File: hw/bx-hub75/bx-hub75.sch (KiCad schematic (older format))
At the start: 11 parts, among them J1 DB9_Male, U1 74HCT541, U2 74HCT541, U3 LD1117S33TR_SOT223, U4 25LCxxx, U5 SN65HVD77D

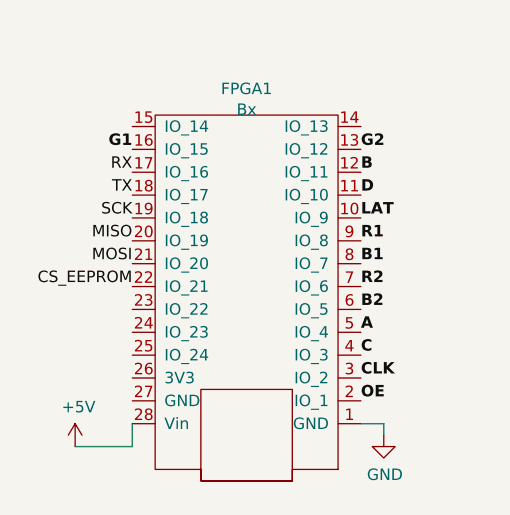
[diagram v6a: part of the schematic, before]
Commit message: hw/bx-hub75: finish basic routing.
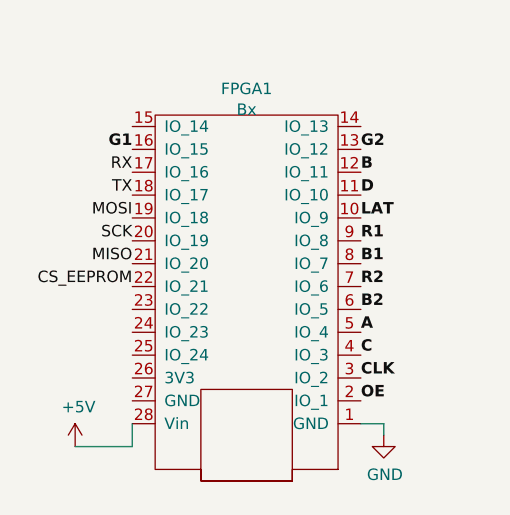
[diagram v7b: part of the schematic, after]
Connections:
- net MISO: now also FPGA1.21 (IO_20); no longer FPGA1.20 (IO_19)
- net MOSI: now also FPGA1.19 (IO_18); no longer FPGA1.21 (IO_20)
- net SCK: now also FPGA1.20 (IO_19); no longer FPGA1.19 (IO_18)
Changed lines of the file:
@@
 Connection ~ 4700 5000
 Text Label 2350 2550 2    50   ~ 0
+MOSI
+Text Label 2350 2650 2    50   ~ 0
 SCK
-Text Label 2350 2650 2    50   ~ 0
+Text Label 2350 2750 2    50   ~ 0
 MISO
-Text Label 2350 2750 2    50   ~ 0
-MOSI
 Text Label 2350 2850 2    50   ~ 0
 CS_EEPROM

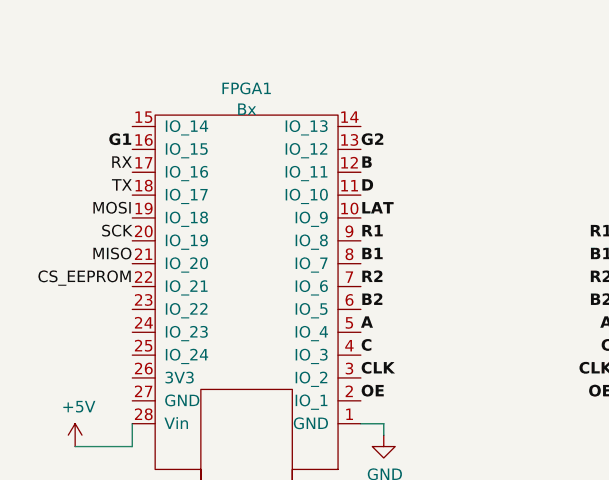
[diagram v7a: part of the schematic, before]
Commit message: hw/{library,bx-hub75}: TinyFPGA has 28 pins, not 26...
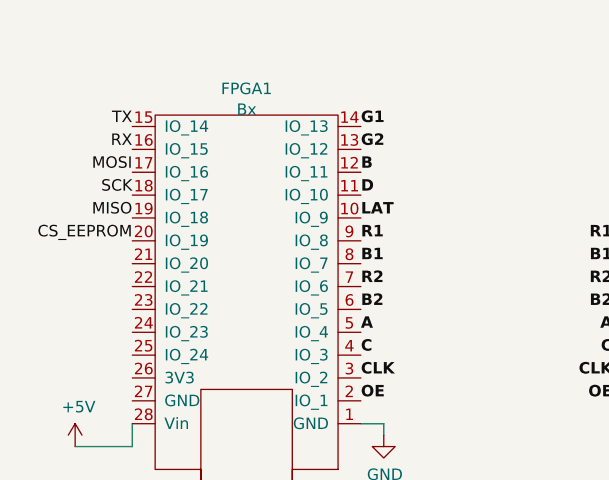
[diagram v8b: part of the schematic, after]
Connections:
- net CS_EEPROM: now also FPGA1.20 (IO_19); no longer FPGA1.22 (IO_21)
- net G1: now also FPGA1.14 (IO_13); no longer FPGA1.16 (IO_15)
- net MISO: now also FPGA1.19 (IO_18); no longer FPGA1.21 (IO_20)
- net MOSI: now also FPGA1.17 (IO_16); no longer FPGA1.19 (IO_18)
- net RX: now also FPGA1.16 (IO_15); no longer FPGA1.17 (IO_16)
- net SCK: now also FPGA1.18 (IO_17); no longer FPGA1.20 (IO_19)
- net TX: now also FPGA1.15 (IO_14); no longer FPGA1.18 (IO_17)
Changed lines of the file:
@@
 Text Label 3350 2250 0    50   ~ 10
 G2
-Text Label 2350 2250 2    50   ~ 10
+Text Label 3350 2150 0    50   ~ 10
 G1
 $Comp
@@
 Wire Wire Line
 	8450 5500 8700 5500
-Text Label 2350 2350 2    50   ~ 0
+Text Label 2350 2150 2    50   ~ 0
+TX
+Text Label 2350 2250 2    50   ~ 0
 RX
-Text Label 2350 2450 2    50   ~ 0
-TX
 $Comp
 L Regulator_Linear:LD1117S33TR_SOT223 U3
@@
 	4700 5100 4700 5000
 Connection ~ 4700 5000
+Text Label 2350 2350 2    50   ~ 0
+MOSI
+Text Label 2350 2450 2    50   ~ 0
+SCK
 Text Label 2350 2550 2    50   ~ 0
-MOSI
+MISO
 Text Label 2350 2650 2    50   ~ 0
-SCK
-Text Label 2350 2750 2    50   ~ 0
-MISO
-Text Label 2350 2850 2    50   ~ 0
 CS_EEPROM
 $Comp
